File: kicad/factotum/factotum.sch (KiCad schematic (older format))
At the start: 18 parts

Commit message: working on schematic
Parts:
- removed J?: SWD, symbol Connector_Generic:Conn_01x04
- added J1: Conn_01x06, symbol Connector_Generic:Conn_01x06
- added R1, R2, R3, R4, R5, R6, R68, R69: 100, symbol Device:R_Small
- gave numbers to parts that had none: 17
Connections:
- net +3V3: now also J1.1 (Pin_1)
- net GND: now also J1.3 (Pin_3)
- net NSRT: now also J1.5 (Pin_5)
- net SWCLK: now also J1.2 (Pin_2)
- net SWDIO: now also J1.4 (Pin_4)
- net at U1.10 (PC2): now also R1.2
- net at U1.11 (PC3): now also R2.2
- net at U1.20 (PA4): now also R69.2
- net B_MODE: now reaches U1.26 (PB0)
- net at U1.51 (PC10): now also R3.2
- net SWO: now reaches U1.55 (PB3)
- net SWO: now also J1.6 (Pin_6)
- net at U1.9 (PC1): now also R68.2
- net I2S1_MISO: no longer names the net of U1.22 (PA6)
- net I2S1_MISO: now also R5.2
- net I2S1_MOSI: no longer names the net of U1.23 (PA7)
- net I2S1_MOSI: now also R6.2
- net SPI1_SCK: no longer names the net of U1.21 (PA5)
- net SPI1_SCK: now also R4.2
- new net ADC_CS: R69.1
- new net DAC_SYNC: R68.1
- new net SPI1_MISO: R5.1
- new net SPI1_MOSI: R6.1
- new net SPI1_SCLK: R4.1
- new net SPI2_MISO: R1.1
- new net SPI2_MOSI: R2.1
- new net SPI2_SCLK: R3.1
- no-connect marks 2 -> 34
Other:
- moved on the sheet: J2, R10, R11, R9

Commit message: initial layout of top board
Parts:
- C1, C2, C3, C4, C5, C6, C7, C8, C9: footprint (none) -> Capacitor_SMD:C_0603_1608Metric_Pad1.08x0.95mm_HandSolder
- J1: footprint (none) -> Connector_PinHeader_1.27mm:PinHeader_1x06_P1.27mm_Vertical
- J2: footprint (none) -> Connector_PinHeader_1.27mm:PinHeader_1x02_P1.27mm_Vertical
- R1, R10, R11, R2, R3, R4, R5, R6, R68, R69, R7, R8, R9: footprint (none) -> Resistor_SMD:R_0201_0603Metric_Pad0.64x0.40mm_HandSolder
- Y1: footprint (none) -> Crystal:Crystal_SMD_0603-4Pin_6.0x3.5mm_HandSoldering
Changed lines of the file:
@@
 F 0 "Y1" V 3954 3344 50  0000 L CNN
 F 1 "16 MHz" V 4045 3344 50  0000 L CNN
-F 2 "" H 4000 3100 50  0001 C CNN
+F 2 "Crystal:Crystal_SMD_0603-4Pin_6.0x3.5mm_HandSoldering" H 4000 3100 50  0001 C CNN
 F 3 "~" H 4000 3100 50  0001 C CNN
 	1    4000 3100
@@
 F 0 "C1" V 3371 2950 50  0000 C CNN
 F 1 "C_Small" V 3462 2950 50  0000 C CNN
-F 2 "" H 3600 2950 50  0001 C CNN
+F 2 "Capacitor_SMD:C_0603_1608Metric_Pad1.08x0.95mm_HandSolder" H 3600 2950 50  0001 C CNN
 F 3 "~" H 3600 2950 50  0001 C CNN
 	1    3600 2950
@@
 F 0 "C2" V 3371 3250 50  0000 C CNN
 F 1 "C_Small" V 3462 3250 50  0000 C CNN
-F 2 "" H 3600 3250 50  0001 C CNN
+F 2 "Capacitor_SMD:C_0603_1608Metric_Pad1.08x0.95mm_HandSolder" H 3600 3250 50  0001 C CNN
 F 3 "~" H 3600 3250 50  0001 C CNN
 	1    3600 3250
@@
 F 0 "C5" H 4450 2400 50  0000 L CNN
 F 1 "1u" H 4450 2300 50  0000 L CNN
-F 2 "" H 4650 2350 50  0001 C CNN
+F 2 "Capacitor_SMD:C_0603_1608Metric_Pad1.08x0.95mm_HandSolder" H 4650 2350 50  0001 C CNN
 F 3 "~" H 4650 2350 50  0001 C CNN
 	1    4650 2350
@@
 F 0 "R7" V 8254 2350 50  0000 C CNN
 F 1 "4.7k" V 8345 2350 50  0000 C CNN
-F 2 "" H 8450 2350 50  0001 C CNN
+F 2 "Resistor_SMD:R_0201_0603Metric_Pad0.64x0.40mm_HandSolder" H 8450 2350 50  0001 C CNN
 F 3 "~" H 8450 2350 50  0001 C CNN
 	1    8450 2350
@@
 F 0 "R8" V 8650 2500 50  0000 C CNN
 F 1 "4.7k" V 8550 2500 50  0000 C CNN
-F 2 "" H 8450 2500 50  0001 C CNN
+F 2 "Resistor_SMD:R_0201_0603Metric_Pad0.64x0.40mm_HandSolder" H 8450 2500 50  0001 C CNN
 F 3 "~" H 8450 2500 50  0001 C CNN
 	1    8450 2500
@@
 F 0 "R9" H 9141 3554 50  0000 R CNN
 F 1 "10k" H 9141 3645 50  0000 R CNN
-F 2 "" H 9200 3600 50  0001 C CNN
+F 2 "Resistor_SMD:R_0201_0603Metric_Pad0.64x0.40mm_HandSolder" H 9200 3600 50  0001 C CNN
 F 3 "~" H 9200 3600 50  0001 C CNN
 	1    9200 3600
@@
 F 0 "J2" H 8300 4300 50  0000 C CNN
 F 1 "USART" V 8400 4450 50  0000 C CNN
-F 2 "" H 8300 4500 50  0001 C CNN
+F 2 "Connector_PinHeader_1.27mm:PinHeader_1x02_P1.27mm_Vertical" H 8300 4500 50  0001 C CNN
 F 3 "~" H 8300 4500 50  0001 C CNN
 	1    8300 4500
@@
 F 0 "R10" V 8554 4400 50  0000 C CNN
 F 1 "100" V 8645 4400 50  0000 C CNN
-F 2 "" H 8750 4400 50  0001 C CNN
+F 2 "Resistor_SMD:R_0201_0603Metric_Pad0.64x0.40mm_HandSolder" H 8750 4400 50  0001 C CNN
 F 3 "~" H 8750 4400 50  0001 C CNN
 	1    8750 4400
@@
 F 0 "R11" V 8950 4500 50  0000 C CNN
 F 1 "100" V 8850 4500 50  0000 C CNN
-F 2 "" H 8750 4500 50  0001 C CNN
+F 2 "Resistor_SMD:R_0201_0603Metric_Pad0.64x0.40mm_HandSolder" H 8750 4500 50  0001 C CNN
 F 3 "~" H 8750 4500 50  0001 C CNN
 	1    8750 4500
@@
 F 0 "C7" H 5000 1550 50  0000 L CNN
 F 1 "1u" H 5000 1450 50  0000 L CNN
-F 2 "" H 5200 1500 50  0001 C CNN
+F 2 "Capacitor_SMD:C_0603_1608Metric_Pad1.08x0.95mm_HandSolder" H 5200 1500 50  0001 C CNN
 F 3 "~" H 5200 1500 50  0001 C CNN
 	1    5200 1500
@@
 F 0 "C6" H 4700 1550 50  0000 L CNN
 F 1 "100n" H 4700 1450 50  0000 L CNN
-F 2 "" H 4900 1500 50  0001 C CNN
+F 2 "Capacitor_SMD:C_0603_1608Metric_Pad1.08x0.95mm_HandSolder" H 4900 1500 50  0001 C CNN
 F 3 "~" H 4900 1500 50  0001 C CNN
 	1    4900 1500
@@
 F 0 "C4" H 4400 1550 50  0000 L CNN
 F 1 "100n" H 4400 1450 50  0000 L CNN
-F 2 "" H 4600 1500 50  0001 C CNN
+F 2 "Capacitor_SMD:C_0603_1608Metric_Pad1.08x0.95mm_HandSolder" H 4600 1500 50  0001 C CNN
 F 3 "~" H 4600 1500 50  0001 C CNN
 	1    4600 1500
@@
 F 0 "C3" H 4100 1550 50  0000 L CNN
 F 1 "1u" H 4100 1450 50  0000 L CNN
-F 2 "" H 4300 1500 50  0001 C CNN
+F 2 "Capacitor_SMD:C_0603_1608Metric_Pad1.08x0.95mm_HandSolder" H 4300 1500 50  0001 C CNN
 F 3 "~" H 4300 1500 50  0001 C CNN
 	1    4300 1500
@@
 F 0 "C8" H 5800 1550 50  0000 L CNN
 F 1 "1u" H 5800 1450 50  0000 L CNN
-F 2 "" H 6000 1500 50  0001 C CNN
+F 2 "Capacitor_SMD:C_0603_1608Metric_Pad1.08x0.95mm_HandSolder" H 6000 1500 50  0001 C CNN
 F 3 "~" H 6000 1500 50  0001 C CNN
 	1    6000 1500
@@
 F 0 "C9" H 6100 1550 50  0000 L CNN
 F 1 "100n" H 6100 1450 50  0000 L CNN
-F 2 "" H 6300 1500 50  0001 C CNN
+F 2 "Capacitor_SMD:C_0603_1608Metric_Pad1.08x0.95mm_HandSolder" H 6300 1500 50  0001 C CNN
 F 3 "~" H 6300 1500 50  0001 C CNN
 	1    6300 1500
@@
 F 0 "R4" V 6500 2300 50  0000 C CNN
 F 1 "100" V 6500 2450 50  0000 C CNN
-F 2 "" H 6500 2450 50  0001 C CNN
+F 2 "Resistor_SMD:R_0201_0603Metric_Pad0.64x0.40mm_HandSolder" H 6500 2450 50  0001 C CNN
 F 3 "~" H 6500 2450 50  0001 C CNN
 	1    6500 2450
@@
 F 0 "R5" V 6500 2400 50  0000 C CNN
 F 1 "100" V 6500 2550 50  0000 C CNN
-F 2 "" H 6500 2550 50  0001 C CNN
+F 2 "Resistor_SMD:R_0201_0603Metric_Pad0.64x0.40mm_HandSolder" H 6500 2550 50  0001 C CNN
 F 3 "~" H 6500 2550 50  0001 C CNN
 	1    6500 2550
@@
 F 0 "R6" V 6500 2500 50  0000 C CNN
 F 1 "100" V 6500 2650 50  0000 C CNN
-F 2 "" H 6500 2650 50  0001 C CNN
+F 2 "Resistor_SMD:R_0201_0603Metric_Pad0.64x0.40mm_HandSolder" H 6500 2650 50  0001 C CNN
 F 3 "~" H 6500 2650 50  0001 C CNN
 	1    6500 2650
@@
 F 0 "R3" V 4700 4400 50  0000 C CNN
 F 1 "100" V 4700 4550 50  0000 C CNN
-F 2 "" H 4700 4550 50  0001 C CNN
+F 2 "Resistor_SMD:R_0201_0603Metric_Pad0.64x0.40mm_HandSolder" H 4700 4550 50  0001 C CNN
 F 3 "~" H 4700 4550 50  0001 C CNN
 	1    4700 4550
@@
 F 0 "R2" V 4700 3700 50  0000 C CNN
 F 1 "100" V 4700 3850 50  0000 C CNN
-F 2 "" H 4700 3850 50  0001 C CNN
+F 2 "Resistor_SMD:R_0201_0603Metric_Pad0.64x0.40mm_HandSolder" H 4700 3850 50  0001 C CNN
 F 3 "~" H 4700 3850 50  0001 C CNN
 	1    4700 3850
@@
 F 0 "R1" V 4700 3600 50  0000 C CNN
 F 1 "100" V 4700 3750 50  0000 C CNN
-F 2 "" H 4700 3750 50  0001 C CNN
+F 2 "Resistor_SMD:R_0201_0603Metric_Pad0.64x0.40mm_HandSolder" H 4700 3750 50  0001 C CNN
 F 3 "~" H 4700 3750 50  0001 C CNN
 	1    4700 3750
@@
 F 0 "J1" H 8218 3175 50  0000 C CNN
 F 1 "Conn_01x06" H 8218 3266 50  0000 C CNN
-F 2 "" H 8300 3700 50  0001 C CNN
+F 2 "Connector_PinHeader_1.27mm:PinHeader_1x06_P1.27mm_Vertical" H 8300 3700 50  0001 C CNN
 F 3 "~" H 8300 3700 50  0001 C CNN
 	1    8300 3700
@@
 F 0 "R69" V 6500 2200 50  0000 C CNN
 F 1 "100" V 6500 2350 50  0000 C CNN
-F 2 "" H 6500 2350 50  0001 C CNN
+F 2 "Resistor_SMD:R_0201_0603Metric_Pad0.64x0.40mm_HandSolder" H 6500 2350 50  0001 C CNN
 F 3 "~" H 6500 2350 50  0001 C CNN
 	1    6500 2350
@@
 F 0 "R68" V 4700 3500 50  0000 C CNN
 F 1 "100" V 4700 3650 50  0000 C CNN
-F 2 "" H 4700 3650 50  0001 C CNN
+F 2 "Resistor_SMD:R_0201_0603Metric_Pad0.64x0.40mm_HandSolder" H 4700 3650 50  0001 C CNN
 F 3 "~" H 4700 3650 50  0001 C CNN
 	1    4700 3650

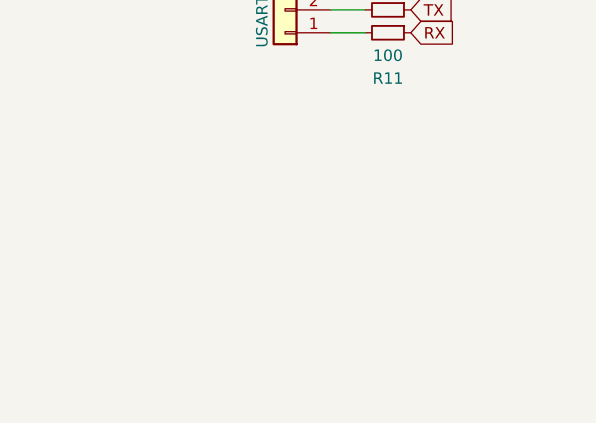
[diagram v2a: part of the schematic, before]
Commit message: inital board layout done but not routed
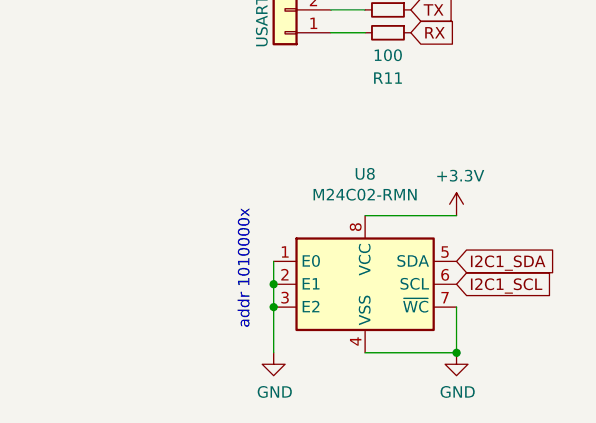
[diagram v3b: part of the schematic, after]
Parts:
- added U8: M24C02-RMN, Package_SO:SOIC-8_3.9x4.9mm_P1.27mm, symbol Memory_EEPROM:M24C02-RMN
- J1: footprint Connector_PinHeader_1.27mm:PinHeader_1x06_P1.27mm_Vertical -> Connector_PinHeader_2.54mm:PinHeader_1x06_P2.54mm_Vertical
- J2: footprint Connector_PinHeader_1.27mm:PinHeader_1x02_P1.27mm_Vertical -> Connector_PinHeader_2.54mm:PinHeader_1x02_P2.54mm_Vertical
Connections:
- net +3V3: now also U8.8 (VCC)
- net GND: now also U8.1 (E0), U8.2 (E1), U8.3 (E2), U8.4 (VSS), U8.7 (~WC)
- net I2C1_SCL: now also U8.6 (SCL)
- net I2C1_SDA: now also U8.5 (SDA)
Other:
- note added: "addr 1010000x"
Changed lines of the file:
@@
 F 0 "J2" H 8300 4300 50  0000 C CNN
 F 1 "USART" V 8400 4450 50  0000 C CNN
-F 2 "Connector_PinHeader_1.27mm:PinHeader_1x02_P1.27mm_Vertical" H 8300 4500 50  0001 C CNN
+F 2 "Connector_PinHeader_2.54mm:PinHeader_1x02_P2.54mm_Vertical" H 8300 4500 50  0001 C CNN
 F 3 "~" H 8300 4500 50  0001 C CNN
 	1    8300 4500
@@
 F 0 "J1" H 8218 3175 50  0000 C CNN
 F 1 "Conn_01x06" H 8218 3266 50  0000 C CNN
-F 2 "Connector_PinHeader_1.27mm:PinHeader_1x06_P1.27mm_Vertical" H 8300 3700 50  0001 C CNN
+F 2 "Connector_PinHeader_2.54mm:PinHeader_1x06_P2.54mm_Vertical" H 8300 3700 50  0001 C CNN
 F 3 "~" H 8300 3700 50  0001 C CNN
 	1    8300 3700
@@
 Text GLabel 6300 3650 2    50   Input ~ 0
 B_MODE
+$Comp
+L Memory_EEPROM:M24C02-RMN U8
+U 1 1 5FCBE0D3
+P 8650 5600
+F 0 "U8" H 8650 6081 50  0000 C CNN
+F 1 "M24C02-RMN" H 8650 5990 50  0000 C CNN
+F 2 "Package_SO:SOIC-8_3.9x4.9mm_P1.27mm" H 8650 5950 50  0001 C CNN
+F 3 "http://www.st.com/content/ccc/resource/technical/document/datasheet/b0/d8/50/40/5a/85/49/6f/DM00071904.pdf/files/DM00071904.pdf/jcr:content/translations/en.DM00071904.pdf" H 8700 5100 50  0001 C CNN
+	1    8650 5600
+	1    0    0    -1
+$EndComp
+Text GLabel 9050 5600 2    50   Input ~ 0
+I2C1_SCL
+Text GLabel 9050 5500 2    50   Input ~ 0
+I2C1_SDA
+$Comp
+L power:GND #PWR096
+U 1 1 5FCC2B30
+P 9050 5900
+F 0 "#PWR096" H 9050 5650 50  0001 C CNN
+F 1 "GND" H 9055 5727 50  0000 C CNN
+F 2 "" H 9050 5900 50  0001 C CNN
+F 3 "" H 9050 5900 50  0001 C CNN
+	1    9050 5900
+	1    0    0    -1
+$EndComp
+$Comp
+L power:+3.3V #PWR095
+U 1 1 5FCC3186
+P 9050 5300
+F 0 "#PWR095" H 9050 5150 50  0001 C CNN
+F 1 "+3.3V" H 9065 5473 50  0000 C CNN
+F 2 "" H 9050 5300 50  0001 C CNN
+F 3 "" H 9050 5300 50  0001 C CNN
+	1    9050 5300
+	1    0    0    -1
+$EndComp
+Wire Wire Line
+	8650 5300 9050 5300
+Wire Wire Line
+	8650 5900 9050 5900
+Text Notes 8150 5800 1    50   ~ 0
+addr 1010000x
+$Comp
+L power:GND #PWR094
+U 1 1 5FCD7888
+P 8250 5900
+F 0 "#PWR094" H 8250 5650 50  0001 C CNN
+F 1 "GND" H 8255 5727 50  0000 C CNN
+F 2 "" H 8250 5900 50  0001 C CNN
+F 3 "" H 8250 5900 50  0001 C CNN
+	1    8250 5900
+	1    0    0    -1
+$EndComp
+Wire Wire Line
+	8250 5500 8250 5600
+Connection ~ 8250 5600
+Wire Wire Line
+	8250 5600 8250 5700
+Connection ~ 8250 5700
+Wire Wire Line
+	8250 5700 8250 5900
+Wire Wire Line
+	9050 5700 9050 5900
+Connection ~ 9050 5900
 $EndSCHEMATC

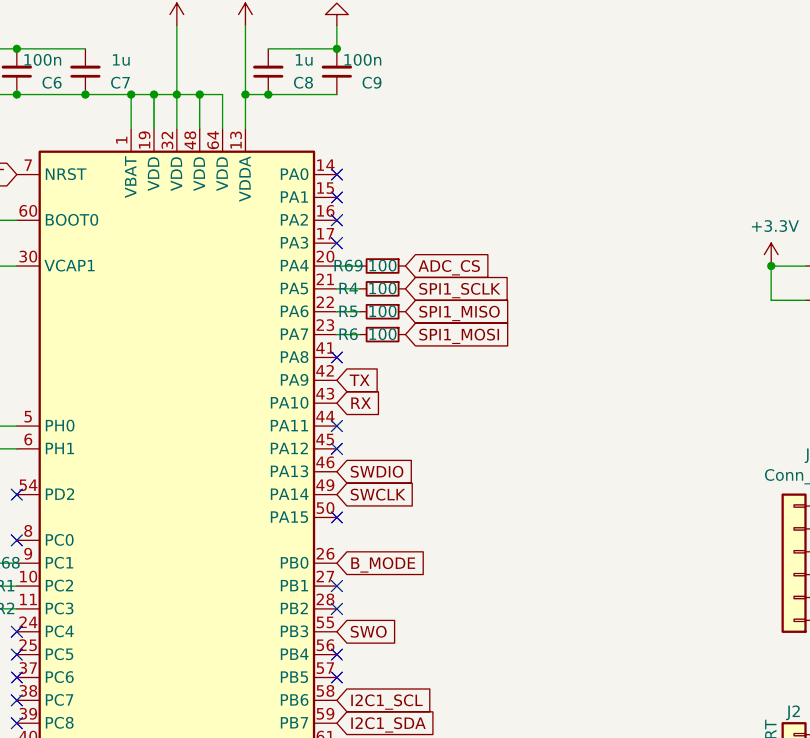
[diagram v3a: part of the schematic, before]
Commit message: adding switches to inputs; fixing resistor components to 603
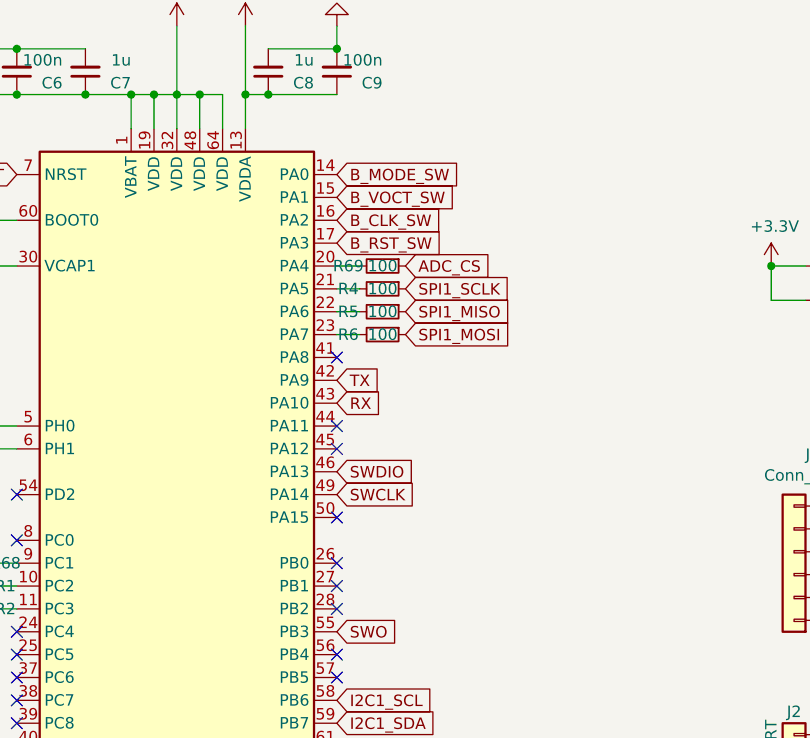
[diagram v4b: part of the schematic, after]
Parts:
- R1, R10, R11, R2, R3, R4, R5, R6, R68, R69, R7, R8, R9: footprint Resistor_SMD:R_0201_0603Metric_Pad0.64x0.40mm_HandSolder -> Resistor_SMD:R_0603_1608Metric_Pad0.98x0.95mm_HandSolder
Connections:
- net B_MODE_SW: now reaches U1.14 (PA0)
- net B_VOCT_SW: now reaches U1.15 (PA1)
- net B_CLK_SW: now reaches U1.16 (PA2)
- net B_RST_SW: now reaches U1.17 (PA3)
- net B_MODE: no longer names the net of U1.26 (PB0)
- no-connect marks 34 -> 31
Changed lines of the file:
@@
 F 0 "R7" V 8254 2350 50  0000 C CNN
 F 1 "4.7k" V 8345 2350 50  0000 C CNN
-F 2 "Resistor_SMD:R_0201_0603Metric_Pad0.64x0.40mm_HandSolder" H 8450 2350 50  0001 C CNN
+F 2 "Resistor_SMD:R_0603_1608Metric_Pad0.98x0.95mm_HandSolder" H 8450 2350 50  0001 C CNN
 F 3 "~" H 8450 2350 50  0001 C CNN
 	1    8450 2350
@@
 F 0 "R8" V 8650 2500 50  0000 C CNN
 F 1 "4.7k" V 8550 2500 50  0000 C CNN
-F 2 "Resistor_SMD:R_0201_0603Metric_Pad0.64x0.40mm_HandSolder" H 8450 2500 50  0001 C CNN
+F 2 "Resistor_SMD:R_0603_1608Metric_Pad0.98x0.95mm_HandSolder" H 8450 2500 50  0001 C CNN
 F 3 "~" H 8450 2500 50  0001 C CNN
 	1    8450 2500
@@
 F 0 "R9" H 9141 3554 50  0000 R CNN
 F 1 "10k" H 9141 3645 50  0000 R CNN
-F 2 "Resistor_SMD:R_0201_0603Metric_Pad0.64x0.40mm_HandSolder" H 9200 3600 50  0001 C CNN
+F 2 "Resistor_SMD:R_0603_1608Metric_Pad0.98x0.95mm_HandSolder" H 9200 3600 50  0001 C CNN
 F 3 "~" H 9200 3600 50  0001 C CNN
 	1    9200 3600
@@
 F 0 "R10" V 8554 4400 50  0000 C CNN
 F 1 "100" V 8645 4400 50  0000 C CNN
-F 2 "Resistor_SMD:R_0201_0603Metric_Pad0.64x0.40mm_HandSolder" H 8750 4400 50  0001 C CNN
+F 2 "Resistor_SMD:R_0603_1608Metric_Pad0.98x0.95mm_HandSolder" H 8750 4400 50  0001 C CNN
 F 3 "~" H 8750 4400 50  0001 C CNN
 	1    8750 4400
@@
 F 0 "R11" V 8950 4500 50  0000 C CNN
 F 1 "100" V 8850 4500 50  0000 C CNN
-F 2 "Resistor_SMD:R_0201_0603Metric_Pad0.64x0.40mm_HandSolder" H 8750 4500 50  0001 C CNN
+F 2 "Resistor_SMD:R_0603_1608Metric_Pad0.98x0.95mm_HandSolder" H 8750 4500 50  0001 C CNN
 F 3 "~" H 8750 4500 50  0001 C CNN
 	1    8750 4500
@@
 F 0 "R4" V 6500 2300 50  0000 C CNN
 F 1 "100" V 6500 2450 50  0000 C CNN
-F 2 "Resistor_SMD:R_0201_0603Metric_Pad0.64x0.40mm_HandSolder" H 6500 2450 50  0001 C CNN
+F 2 "Resistor_SMD:R_0603_1608Metric_Pad0.98x0.95mm_HandSolder" H 6500 2450 50  0001 C CNN
 F 3 "~" H 6500 2450 50  0001 C CNN
 	1    6500 2450
@@
 F 0 "R5" V 6500 2400 50  0000 C CNN
 F 1 "100" V 6500 2550 50  0000 C CNN
-F 2 "Resistor_SMD:R_0201_0603Metric_Pad0.64x0.40mm_HandSolder" H 6500 2550 50  0001 C CNN
+F 2 "Resistor_SMD:R_0603_1608Metric_Pad0.98x0.95mm_HandSolder" H 6500 2550 50  0001 C CNN
 F 3 "~" H 6500 2550 50  0001 C CNN
 	1    6500 2550
@@
 F 0 "R6" V 6500 2500 50  0000 C CNN
 F 1 "100" V 6500 2650 50  0000 C CNN
-F 2 "Resistor_SMD:R_0201_0603Metric_Pad0.64x0.40mm_HandSolder" H 6500 2650 50  0001 C CNN
+F 2 "Resistor_SMD:R_0603_1608Metric_Pad0.98x0.95mm_HandSolder" H 6500 2650 50  0001 C CNN
 F 3 "~" H 6500 2650 50  0001 C CNN
 	1    6500 2650
@@
 F 0 "R3" V 4700 4400 50  0000 C CNN
 F 1 "100" V 4700 4550 50  0000 C CNN
-F 2 "Resistor_SMD:R_0201_0603Metric_Pad0.64x0.40mm_HandSolder" H 4700 4550 50  0001 C CNN
+F 2 "Resistor_SMD:R_0603_1608Metric_Pad0.98x0.95mm_HandSolder" H 4700 4550 50  0001 C CNN
 F 3 "~" H 4700 4550 50  0001 C CNN
 	1    4700 4550
@@
 F 0 "R2" V 4700 3700 50  0000 C CNN
 F 1 "100" V 4700 3850 50  0000 C CNN
-F 2 "Resistor_SMD:R_0201_0603Metric_Pad0.64x0.40mm_HandSolder" H 4700 3850 50  0001 C CNN
+F 2 "Resistor_SMD:R_0603_1608Metric_Pad0.98x0.95mm_HandSolder" H 4700 3850 50  0001 C CNN
 F 3 "~" H 4700 3850 50  0001 C CNN
 	1    4700 3850
@@
 F 0 "R1" V 4700 3600 50  0000 C CNN
 F 1 "100" V 4700 3750 50  0000 C CNN
-F 2 "Resistor_SMD:R_0201_0603Metric_Pad0.64x0.40mm_HandSolder" H 4700 3750 50  0001 C CNN
+F 2 "Resistor_SMD:R_0603_1608Metric_Pad0.98x0.95mm_HandSolder" H 4700 3750 50  0001 C CNN
 F 3 "~" H 4700 3750 50  0001 C CNN
 	1    4700 3750
@@
 Wire Wire Line
 	4800 4550 4900 4550
-NoConn ~ 6300 1950
-NoConn ~ 6300 2050
-NoConn ~ 6300 2150
-NoConn ~ 6300 2250
 NoConn ~ 6300 2750
 NoConn ~ 6300 3050
@@
 F 0 "R69" V 6500 2200 50  0000 C CNN
 F 1 "100" V 6500 2350 50  0000 C CNN
-F 2 "Resistor_SMD:R_0201_0603Metric_Pad0.64x0.40mm_HandSolder" H 6500 2350 50  0001 C CNN
+F 2 "Resistor_SMD:R_0603_1608Metric_Pad0.98x0.95mm_HandSolder" H 6500 2350 50  0001 C CNN
 F 3 "~" H 6500 2350 50  0001 C CNN
 	1    6500 2350
@@
 F 0 "R68" V 4700 3500 50  0000 C CNN
 F 1 "100" V 4700 3650 50  0000 C CNN
-F 2 "Resistor_SMD:R_0201_0603Metric_Pad0.64x0.40mm_HandSolder" H 4700 3650 50  0001 C CNN
+F 2 "Resistor_SMD:R_0603_1608Metric_Pad0.98x0.95mm_HandSolder" H 4700 3650 50  0001 C CNN
 F 3 "~" H 4700 3650 50  0001 C CNN
 	1    4700 3650
@@
 Wire Wire Line
 	4800 3650 4900 3650
-Text GLabel 6300 3650 2    50   Input ~ 0
-B_MODE
+Text GLabel 6300 1950 2    50   Input ~ 0
+B_MODE_SW
 $Comp
 L Memory_EEPROM:M24C02-RMN U8
@@
 	9050 5700 9050 5900
 Connection ~ 9050 5900
+Text GLabel 6300 2050 2    50   Input ~ 0
+B_VOCT_SW
+Text GLabel 6300 2150 2    50   Input ~ 0
+B_CLK_SW
+Text GLabel 6300 2250 2    50   Input ~ 0
+B_RST_SW
+NoConn ~ 6300 3650
 $EndSCHEMATC
